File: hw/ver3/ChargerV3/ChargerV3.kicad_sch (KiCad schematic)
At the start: 28 parts, among them J1 Terminal Block, J2 Terminal Block, U1 INA180A4, U19 INA180A4

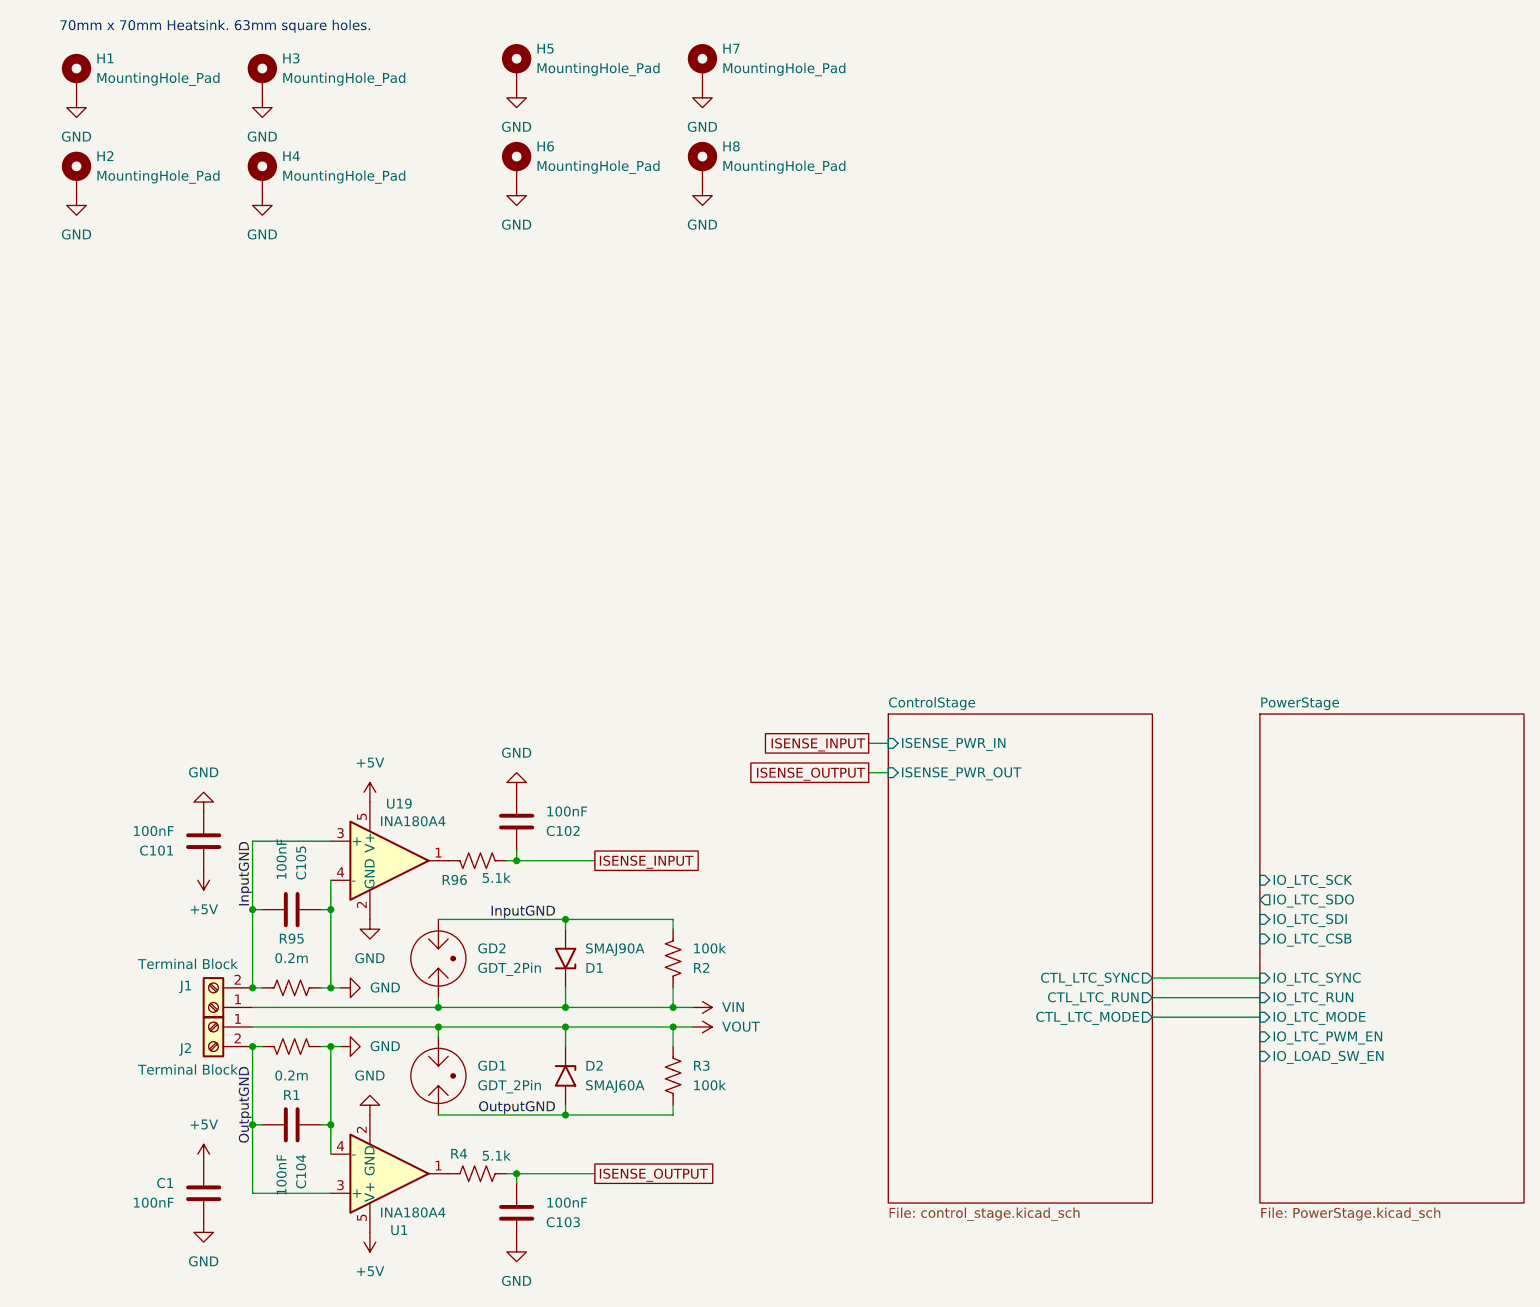
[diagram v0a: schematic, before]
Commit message: Split the design into four major components. Start working on system architecture.
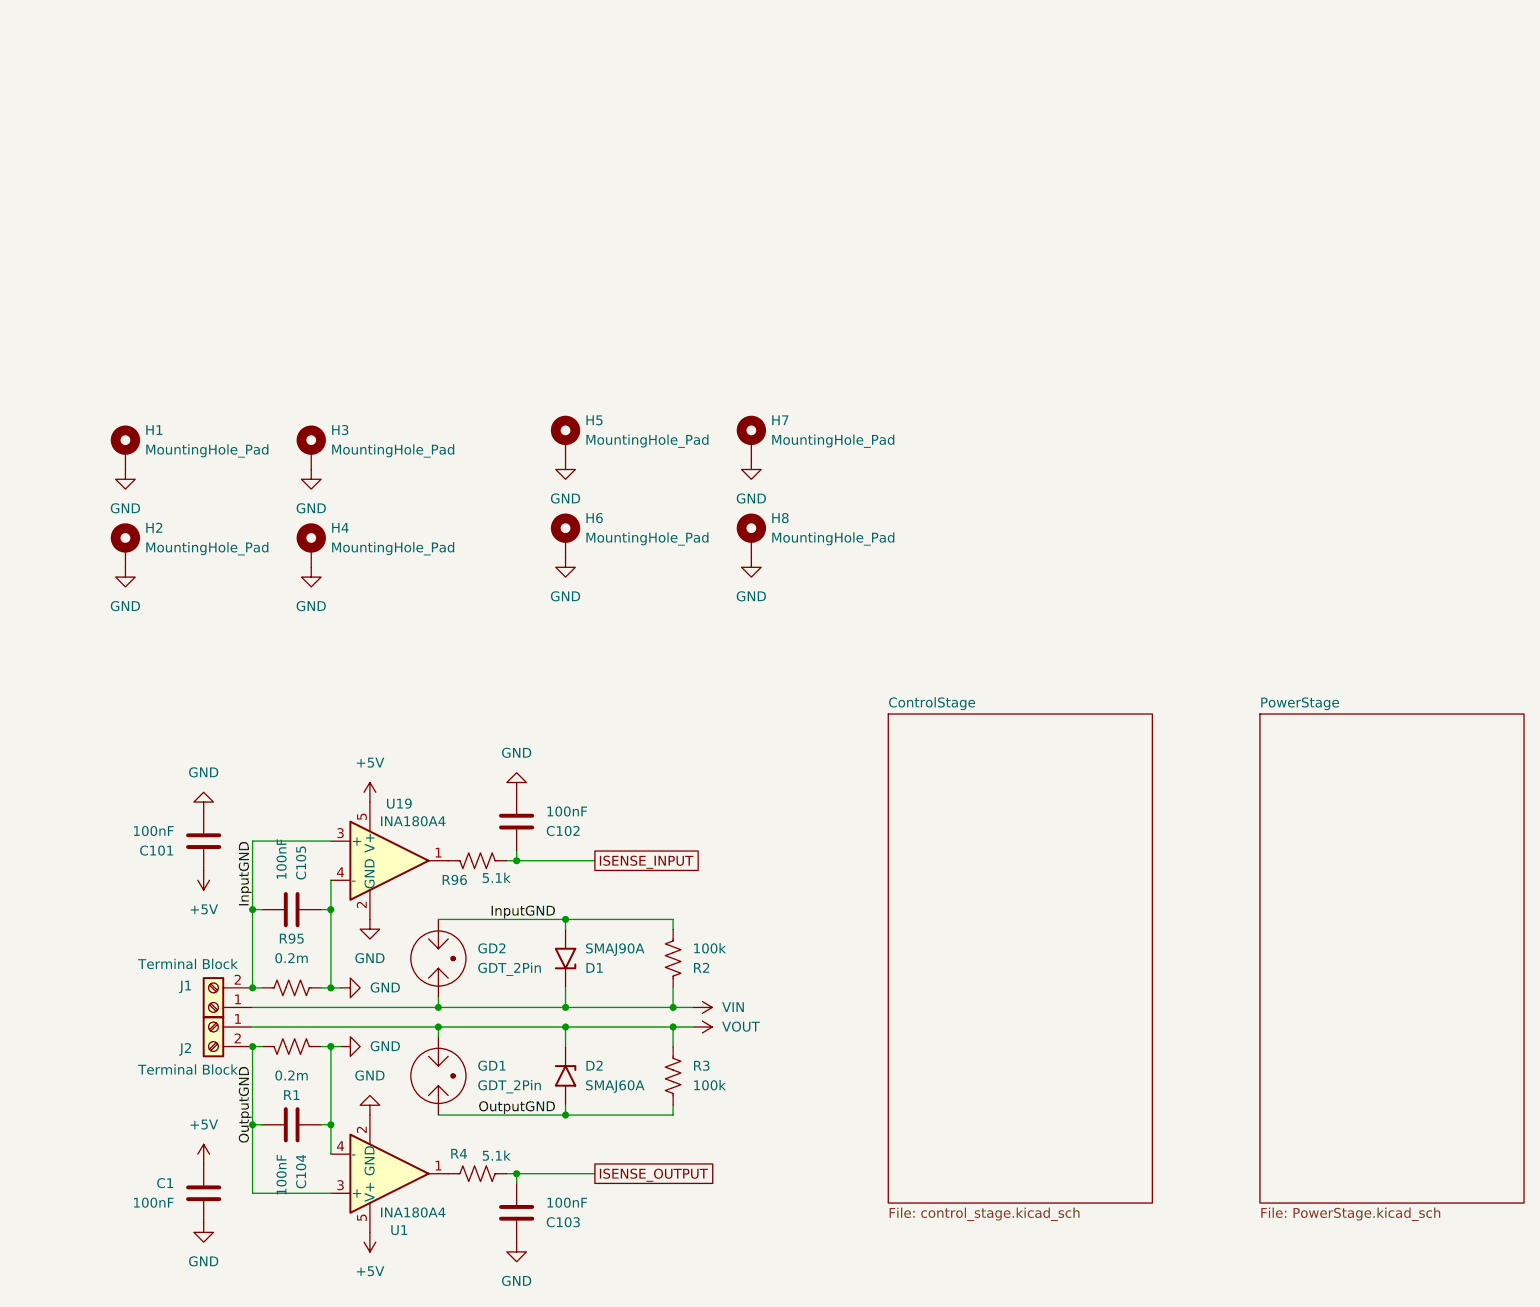
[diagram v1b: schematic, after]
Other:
- sheet ControlStage ports: added none; removed CTL_LTC_MODE, CTL_LTC_RUN, CTL_LTC_SYNC, ISENSE_PWR_IN, ISENSE_PWR_OUT
- sheet PowerStage ports: added none; removed IO_LOAD_SW_EN, IO_LTC_CSB, IO_LTC_MODE, IO_LTC_PWM_EN, IO_LTC_RUN, IO_LTC_SCK, IO_LTC_SDI, IO_LTC_SDO, IO_LTC_SYNC
- note removed: "70mm x 70mm Heatsink. 63mm square holes."
- moved on the sheet: H1, H2, H3, H4, H5, H6, H7, H8

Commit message: Nearly final charger schematic, updated with RS485 interconnect.
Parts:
- removed H4, H5, H6, H7, H8: MountingHole_Pad, MountingHole:MountingHole_3.2mm_M3_Pad_Via, symbol Mechanical:MountingHole_Pad

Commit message: Sync board changes from before work started
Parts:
- removed H1, H2: MountingHole_Pad, MountingHole:MountingHole_3.2mm_M3_Pad_Via, symbol Mechanical:MountingHole_Pad
